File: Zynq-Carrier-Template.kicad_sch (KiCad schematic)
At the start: 5 parts, among them J1 Zynq_SoM

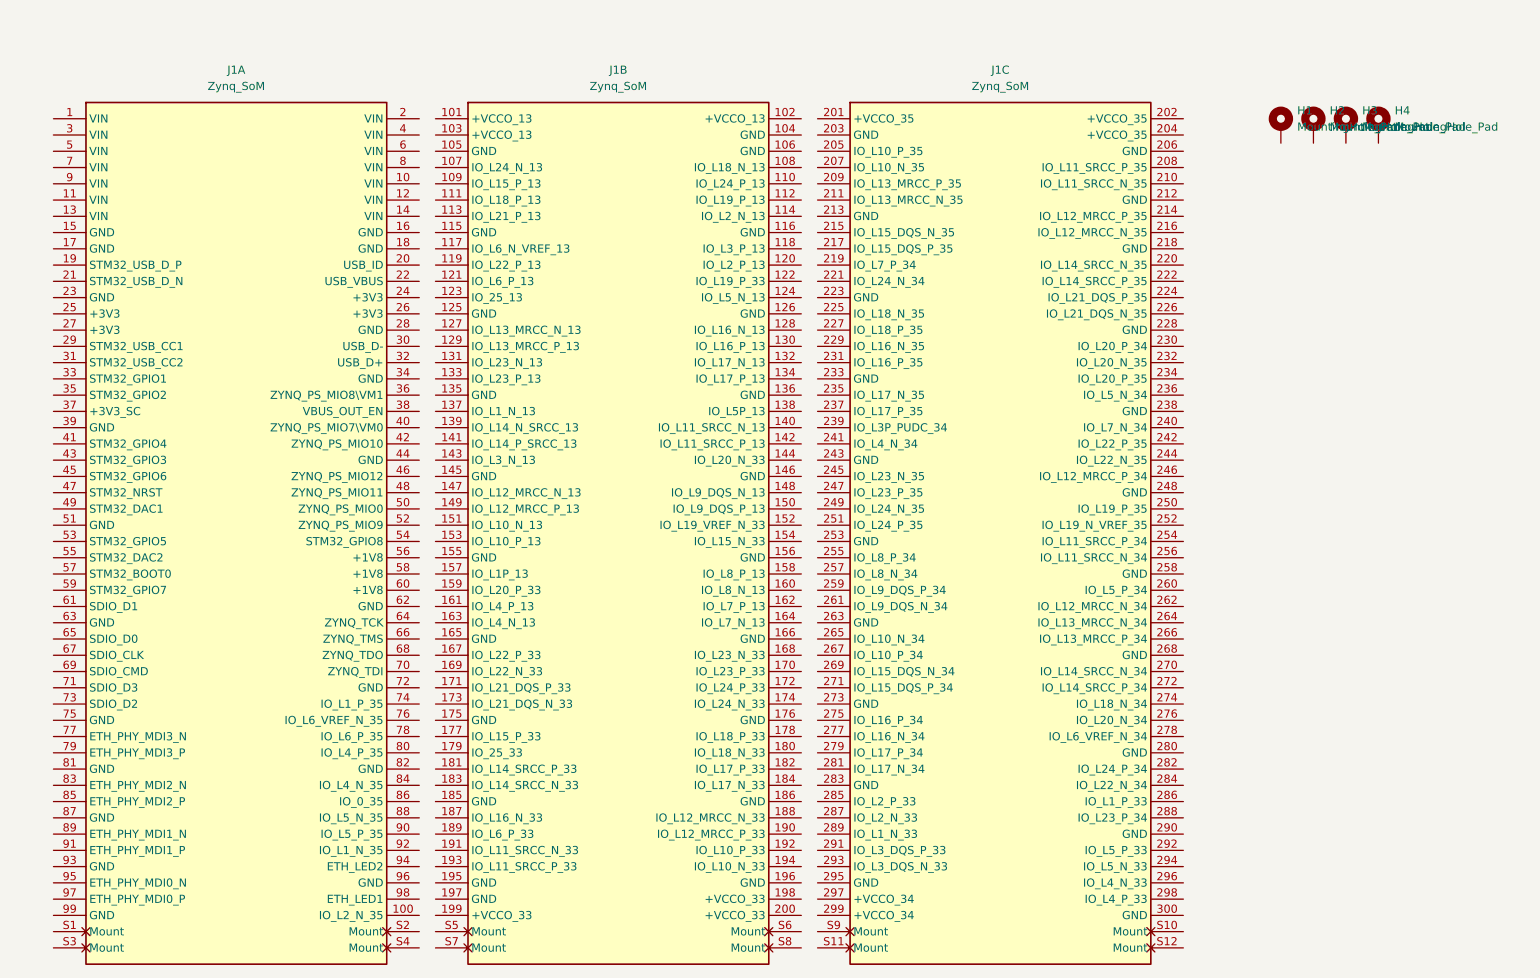
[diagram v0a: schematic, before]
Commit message: Renamed and Updated Silkscreen
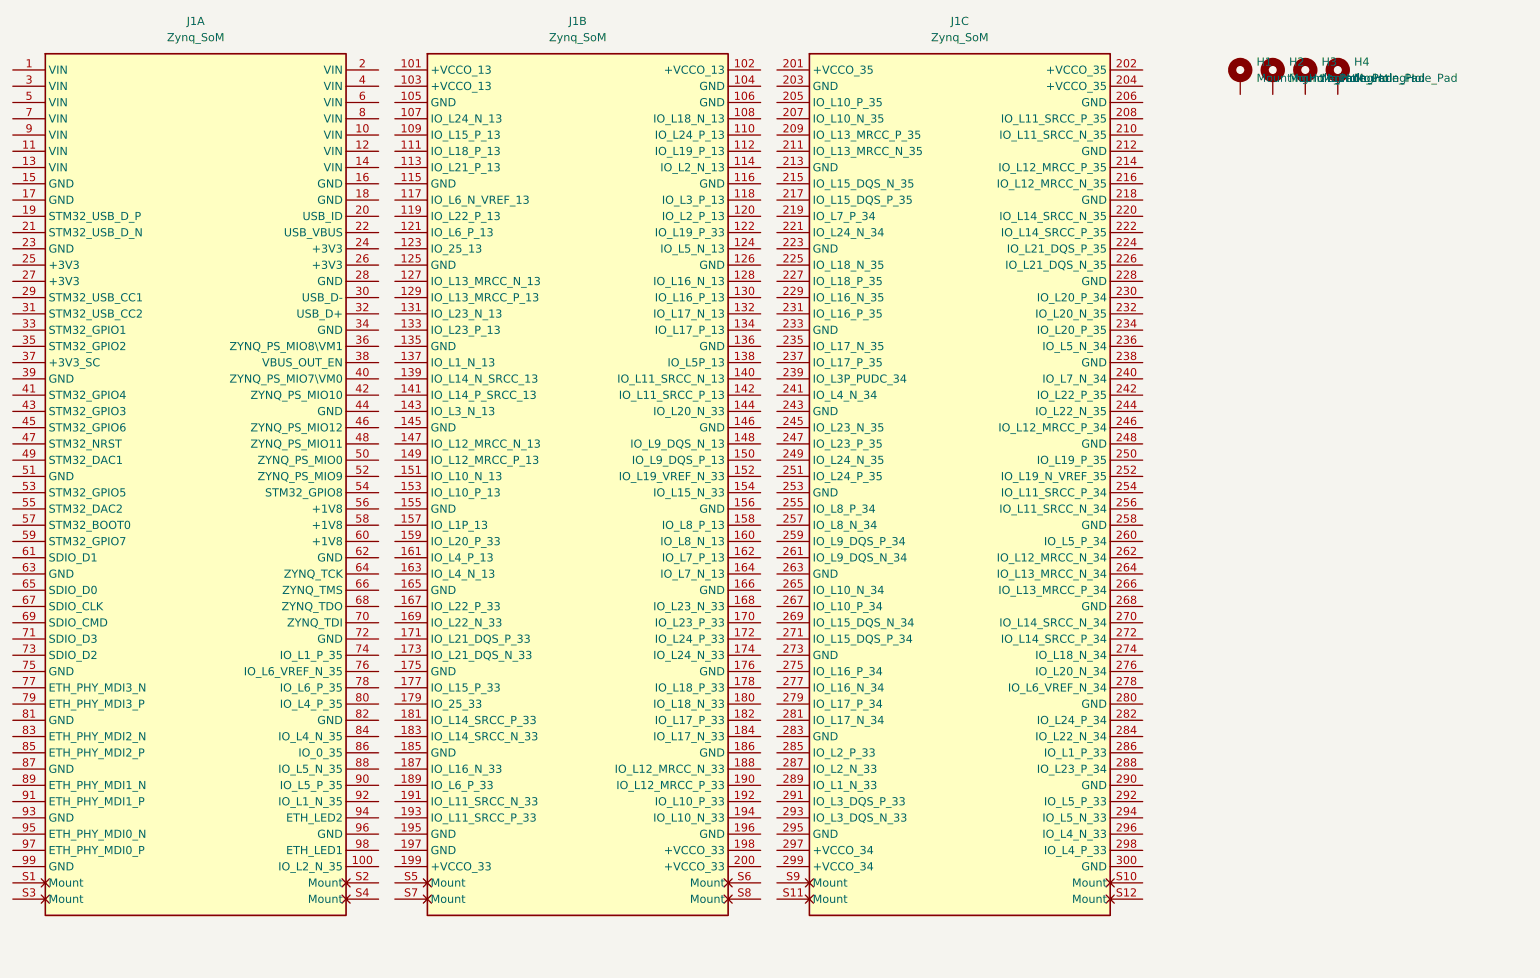
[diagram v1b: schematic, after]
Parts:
- J1: footprint footprint_Zynq_SoM:Zync_SoM -> footprint_Zynq_SoM:Zynq_SoM
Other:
- moved on the sheet: H1, H2, H3, H4, J1A, J1B, J1C
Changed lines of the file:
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@@
 	(symbol
 		(lib_id "Mechanical:MountingHole_Pad")
-		(at 220.98 36.83 0)
+		(at 214.63 29.21 0)
 		(unit 1)
 		(exclude_from_sim yes)
@@
 		(fields_autoplaced yes)
 		(property "Reference" "H1"
-			(at 223.52 34.2899 0)
+			(at 217.17 26.6699 0)
 			(effects
 				(font
@@
 		)
 		(property "Value" "MountingHole_Pad"
-			(at 223.52 36.8299 0)
+			(at 217.17 29.2099 0)
 			(effects
 				(font
@@
 		)
 		(property "Footprint" "MountingHole:MountingHole_2.5mm_Pad_TopBottom"
-			(at 220.98 36.83 0)
+			(at 214.63 29.21 0)
 			(effects
 				(font
@@
 		)
 		(property "Datasheet" "~"
-			(at 220.98 36.83 0)
+			(at 214.63 29.21 0)
 			(effects
 				(font
@@
 		)
 		(property "Description" "Mounting Hole with connection"
-			(at 220.98 36.83 0)
+			(at 214.63 29.21 0)
 			(effects
 				(font
@@
 	(symbol
 		(lib_id "symbol_Zynq_SoM:Zynq_SoM")
-		(at 88.9 35.56 0)
+		(at 82.55 27.94 0)
 		(unit 2)
 		(exclude_from_sim no)
@@
 		(fields_autoplaced yes)
 		(property "Reference" "J1"
-			(at 117.475 27.94 0)
+			(at 111.125 20.32 0)
 			(effects
 				(font
@@
 		)
 		(property "Value" "Zynq_SoM"
-			(at 117.475 30.48 0)
-			(effects
-				(font
-					(size 1.27 1.27)
-				)
-			)
-		)
-		(property "Footprint" "footprint_Zynq_SoM:Zync_SoM"
-			(at 93.98 34.29 0)
+			(at 111.125 22.86 0)
+			(effects
+				(font
+					(size 1.27 1.27)
+				)
+			)
+		)
+		(property "Footprint" "footprint_Zynq_SoM:Zynq_SoM"
+			(at 87.63 26.67 0)
 			(effects
 				(font
@@
 		)
 		(property "Datasheet" ""
-			(at 93.98 39.37 0)
+			(at 87.63 31.75 0)
 			(effects
 				(font
@@
 		)
 		(property "Description" ""
-			(at 88.9 35.56 0)
+			(at 82.55 27.94 0)
 			(effects
 				(font
@@
 	(symbol
 		(lib_id "symbol_Zynq_SoM:Zynq_SoM")
-		(at 29.21 35.56 0)
+		(at 22.86 27.94 0)
 		(unit 1)
 		(exclude_from_sim no)
@@
 		(fields_autoplaced yes)
 		(property "Reference" "J1"
-			(at 57.785 27.94 0)
+			(at 51.435 20.32 0)
 			(effects
 				(font
@@
 		)
 		(property "Value" "Zynq_SoM"
-			(at 57.785 30.48 0)
-			(effects
-				(font
-					(size 1.27 1.27)
-				)
-			)
-		)
-		(property "Footprint" "footprint_Zynq_SoM:Zync_SoM"
-			(at 34.29 34.29 0)
+			(at 51.435 22.86 0)
+			(effects
+				(font
+					(size 1.27 1.27)
+				)
+			)
+		)
+		(property "Footprint" "footprint_Zynq_SoM:Zynq_SoM"
+			(at 27.94 26.67 0)
 			(effects
 				(font
@@
 		)
 		(property "Datasheet" ""
-			(at 34.29 39.37 0)
+			(at 27.94 31.75 0)
 			(effects
 				(font
@@
 		)
 		(property "Description" ""
-			(at 29.21 35.56 0)
+			(at 22.86 27.94 0)
 			(effects
 				(font
@@
 	(symbol
 		(lib_id "Mechanical:MountingHole_Pad")
-		(at 226.06 36.83 0)
+		(at 219.71 29.21 0)
 		(unit 1)
 		(exclude_from_sim yes)
@@
 		(fields_autoplaced yes)
 		(property "Reference" "H2"
-			(at 228.6 34.2899 0)
+			(at 222.25 26.6699 0)
 			(effects
 				(font
@@
 		)
 		(property "Value" "MountingHole_Pad"
-			(at 228.6 36.8299 0)
+			(at 222.25 29.2099 0)
 			(effects
 				(font
@@
 		)
 		(property "Footprint" "MountingHole:MountingHole_2.5mm_Pad_TopBottom"
-			(at 226.06 36.83 0)
+			(at 219.71 29.21 0)
 			(effects
 				(font
@@
 		)
 		(property "Datasheet" "~"
-			(at 226.06 36.83 0)
+			(at 219.71 29.21 0)
 			(effects
 				(font
@@
 		)
 		(property "Description" "Mounting Hole with connection"
-			(at 226.06 36.83 0)
+			(at 219.71 29.21 0)
 			(effects
 				(font
@@
 	(symbol
 		(lib_id "symbol_Zynq_SoM:Zynq_SoM")
-		(at 148.59 35.56 0)
+		(at 142.24 27.94 0)
 		(unit 3)
 		(exclude_from_sim no)
@@
 		(fields_autoplaced yes)
 		(property "Reference" "J1"
-			(at 177.165 27.94 0)
+			(at 170.815 20.32 0)
 			(effects
 				(font
@@
 		)
 		(property "Value" "Zynq_SoM"
-			(at 177.165 30.48 0)
-			(effects
-				(font
-					(size 1.27 1.27)
-				)
-			)
-		)
-		(property "Footprint" "footprint_Zynq_SoM:Zync_SoM"
-			(at 153.67 34.29 0)
+			(at 170.815 22.86 0)
+			(effects
+				(font
+					(size 1.27 1.27)
+				)
+			)
+		)
+		(property "Footprint" "footprint_Zynq_SoM:Zynq_SoM"
+			(at 147.32 26.67 0)
 			(effects
 				(font
@@
 		)
 		(property "Datasheet" ""
-			(at 153.67 39.37 0)
+			(at 147.32 31.75 0)
 			(effects
 				(font
@@
 		)
 		(property "Description" ""
-			(at 148.59 35.56 0)
+			(at 142.24 27.94 0)
 			(effects
 				(font
@@
 	(symbol
 		(lib_id "Mechanical:MountingHole_Pad")
-		(at 236.22 36.83 0)
+		(at 229.87 29.21 0)
 		(unit 1)
 		(exclude_from_sim yes)
@@
 		(fields_autoplaced yes)
 		(property "Reference" "H4"
-			(at 238.76 34.2899 0)
+			(at 232.41 26.6699 0)
 			(effects
 				(font
@@
 		)
 		(property "Value" "MountingHole_Pad"
-			(at 238.76 36.8299 0)
+			(at 232.41 29.2099 0)
 			(effects
 				(font
@@
 		)
 		(property "Footprint" "MountingHole:MountingHole_2.5mm_Pad_TopBottom"
-			(at 236.22 36.83 0)
+			(at 229.87 29.21 0)
 			(effects
 				(font
@@
 		)
 		(property "Datasheet" "~"
-			(at 236.22 36.83 0)
+			(at 229.87 29.21 0)
 			(effects
 				(font
@@
 		)
 		(property "Description" "Mounting Hole with connection"
-			(at 236.22 36.83 0)
+			(at 229.87 29.21 0)
 			(effects
 				(font
@@
 	(symbol
 		(lib_id "Mechanical:MountingHole_Pad")
-		(at 231.14 36.83 0)
+		(at 224.79 29.21 0)
 		(unit 1)
 		(exclude_from_sim yes)
@@
 		(fields_autoplaced yes)
 		(property "Reference" "H3"
-			(at 233.68 34.2899 0)
+			(at 227.33 26.6699 0)
 			(effects
 				(font
@@
 		)
 		(property "Value" "MountingHole_Pad"
-			(at 233.68 36.8299 0)
+			(at 227.33 29.2099 0)
 			(effects
 				(font
@@
 		)
 		(property "Footprint" "MountingHole:MountingHole_2.5mm_Pad_TopBottom"
-			(at 231.14 36.83 0)
+			(at 224.79 29.21 0)
 			(effects
 				(font
@@
 		)
 		(property "Datasheet" "~"
-			(at 231.14 36.83 0)
+			(at 224.79 29.21 0)
 			(effects
 				(font
@@
 		)
 		(property "Description" "Mounting Hole with connection"
-			(at 231.14 36.83 0)
-			(effects
-				(font
+			(at 224.79 29.21 0)
+			(effects
+				(font

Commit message: Squashed commit of the following:
commit 0ad81e69922d32d90721302da68770b5998e2075
Author: pixelatedknight27 <97324570+pixelatedknight27@users.noreply.github.com>
Date:   Wed Aug 6 21:23:02 2025 -0700

    Updated Schematic Switching Regulator Output

commit 8c5282f5a799869a6680777a751af97c305c1966
Author: pixelatedknight27 <maxgross72@gmail.com>
Date:   Wed Jul 30 20:10:45 2025 -0700

    Update Zynq-Carrier-Template.kicad_sch

commit 26cabaedd7311c8d419e12e3f1b26bb927437d1c
Author: pixelatedknight27 <maxgross72@gmail.com>
Date:   Mon Jul 28 15:39:58 2025 -0700

    USB-C Schematic

commit 567233bdd00da02cf27e0d5899afb089722db7fc
Author: eryn-chen <eryncchen@gmail.com>
Date:   Mon Jul 28 14:22:40 2025 -0700

    Import JST_Pins and Inductor

commit 3602218fdc51fd4931fe5a5e7236fe1a478a1e89
Author: pixelatedknight27 <maxgross72@gmail.com>
Date:   Mon Jul 28 13:23:57 2025 -0700

    Added USB-C 3D Model

commit c19733a7ca3310077a98ec0354747d6a3ff68208
Author: eryn-chen <eryncchen@gmail.com>
Date:   Mon Jul 28 12:24:48 2025 -0700

    Import 1uH Inductor

commit dad55b1c15193570489f17efb0b30454465aa197
Author: eryn-chen <eryncchen@gmail.com>
Date:   Sat Jul 26 14:08:40 2025 -0700

    3D Model BQ25629RYKR

commit dfd47739e77adc946db50dcb065d6cd1934a3439
Author: pixelatedknight27 <maxgross72@gmail.com>
Date:   Sat Jul 26 13:56:00 2025 -0700

    Copper Fill demo

commit f9846dcb156c9f426159bf7a8c796c584a4552c7
Author: eryn-chen <eryncchen@gmail.com>
Date:   Sat Jul 26 13:32:59 2025 -0700

    Import BQ25629RYKR

commit 6a2dc9275e746e519794c77d9ef984bae5f9a809
Author: pixelatedknight27 <maxgross72@gmail.com>
Date:   Sat Jul 26 12:43:25 2025 -0700

    Testing collab functionality
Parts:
- added C1, C3, C5: 10uf, Capacitor_SMD:C_0603_1608Metric, symbol Device:C
- added C2, C4, C6: 0.1uf, Capacitor_SMD:C_0603_1608Metric, symbol Device:C
- added C7: 4.7 uF, Capacitor_SMD:C_0603_1608Metric, symbol Device:C_Small
- added C8: 47 nF, Capacitor_SMD:C_0603_1608Metric, symbol Device:C_Small
- added D1: LED, LED_SMD:LED_0805_2012Metric, symbol Device:LED
- added J10: Barrel_Jack_MountingPin, Connector_BarrelJack:BarrelJack_Horizontal, symbol Connector:Barrel_Jack_MountingPin
- added J2: B2B-PH-K-S, JST_Pins:CONN2_B2B-PH-K-S_JST, symbol JST_Pins:B2B-PH-K-S
- added J3: USB_C_Receptacle_USB2.0_16P, Connector_USB:USB_C_Receptacle_G-Switch_GT-USB-7010ASV, symbol Connector:USB_C_Receptacle_USB2.0_16P
- added J4, J5, J6, J9: Conn_01x03, Connector_PinHeader_2.54mm:PinHeader_1x03_P2.54mm_Vertical, symbol Connector_Generic:Conn_01x03
- added J7, J8: Conn_01x02, Connector_PinHeader_2.54mm:PinHeader_1x02_P2.54mm_Vertical, symbol Connector_Generic:Conn_01x02
- added L1: L, Inductor_SMD:L_1008_2520Metric_Pad1.43x2.20mm_HandSolder, symbol Device:L
- added R1, R2, R3: 5.1k, Resistor_SMD:R_0603_1608Metric, symbol Device:R_US
- added R10, R7: 10K, Resistor_SMD:R_0603_1608Metric, symbol Device:R_US
- added R11, R8, R9: 4.7k, Resistor_SMD:R_0603_1608Metric, symbol Device:R_US
- added R4: 1M, Resistor_SMD:R_0603_1608Metric, symbol Device:R_US
- added R5: 100k, Resistor_SMD:R_0603_1608Metric, symbol Device:R_US
- added R6: 330, Resistor_SMD:R_0603_1608Metric, symbol Device:R_US
- added U1: BQ25629RYKR, BQ25629RYKR:RYK0018A-MFG, symbol BQ25629RYKR:BQ25629RYKR
- added U12: SRV05-4, Package_TO_SOT_SMD:SOT-23-6, symbol Power_Protection:SRV05-4
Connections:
- net GND: now reaches H1.1
- net GND: now also H2.1, H3.1, H4.1, J1.104 (GND), J1.105 (GND), J1.106 (GND), J1.115 (GND), J1.116 (GND), J1.125 (GND), J1.126 (GND), J1.135 (GND), J1.136 (GND), J1.145 (GND), J1.146 (GND), J1.15 (GND), J1.155 (GND), J1.16 (GND), J1.165 (GND), J1.166 (GND), J1.17 (GND), J1.175 (GND), J1.176 (GND), J1.18 (GND), J1.185 (GND), J1.186 (GND), J1.195 (GND), J1.196 (GND), J1.197 (GND), J1.203 (GND), J1.206 (GND), J1.213 (GND), J1.218 (GND), J1.223 (GND), J1.228 (GND), J1.23 (GND), J1.233 (GND), J1.238 (GND), J1.243 (GND), J1.248 (GND), J1.253 (GND), J1.258 (GND), J1.263 (GND), J1.268 (GND), J1.273 (GND), J1.28 (GND), J1.280 (GND), J1.283 (GND), J1.290 (GND), J1.295 (GND), J1.300 (GND), J1.39 (GND), J1.44 (GND), J1.51 (GND), J1.62 (GND), J1.63 (GND), J1.72 (GND), J1.75 (GND), J1.81 (GND), J1.82 (GND), J1.87 (GND), J1.96 (GND), J1.99 (GND), C1.2, C2.2, C3.2, C4.2, C5.2, C6.2, C7.2, D1.1 (K), J10.2, J10.MP (MountPin), J2.1, J3.A1 (GND), J3.A12 (GND), J3.B1 (GND), J3.B12 (GND), J6.3 (Pin_3), R1.1, R2.1, R4.2, R5.2, U1.15 (GND), U1.6 (TS), U12.2 (VN)
- net +5V: now reaches J1.1 (VIN)
- net +5V: now also J1.10 (VIN), J1.11 (VIN), J1.12 (VIN), J1.13 (VIN), J1.14 (VIN), J1.2 (VIN), J1.3 (VIN), J1.4 (VIN), J1.5 (VIN), J1.6 (VIN), J1.7 (VIN), J1.8 (VIN), J1.9 (VIN), J9.2 (Pin_2), R11.2, R8.1, R9.1
- net USB_SOM_D-: now reaches J1.30 (USB_D-)
- net USB_SOM_D-: now also J4.3 (Pin_3)
- net USB_SOM_D+: now reaches J1.32 (USB_D+)
- net USB_SOM_D+: now also J5.3 (Pin_3)
- new net: J3.A5 (CC1), R1.2
- new net: J3.B5 (CC2), R2.2
- new net: J3.S1 (SHIELD), R4.1
- new net: J7.1 (Pin_1), R8.2
- new net: C8.2, U1.1 (BTST)
- new net: R6.1, U1.10 (STAT)
- new net: C8.1, L1.1, U1.16 (SW)
- new net: C1.1, C2.1, U1.17 (PMID)
- new net: C7.1, U1.2 (REGN)
- new net: J8.1 (Pin_1), R9.2
- new net: R3.2, U12.5 (VP)
- new net: D1.2 (A), R6.2
- new net: J6.1 (Pin_1), R7.2
- new net: J6.2 (Pin_2), R10.2
- new net SCL: J7.2 (Pin_2), R7.1, U1.13 (SCL)
- new net SDA: J8.2 (Pin_2), R10.1, U1.12 (SDA)
- new net USB_D+: J3.A6 (D+), J3.B6 (D+), J5.2 (Pin_2), U12.3 (IO2)
- new net USB_D-: J3.A7 (D-), J3.B7 (D-), J4.2 (Pin_2), U12.1 (IO1)
- new net USB_POW_D+: J5.1 (Pin_1), U1.5 (D+)
- new net USB_POW_D-: J4.1 (Pin_1), U1.4 (D-)
- new net VBAT: J2.2, U1.8 (BAT)
- new net VREG_OUT: J9.1 (Pin_1), L1.2, U1.9 (SYS)
- new net V_USB: C3.1, C4.1, C5.1, C6.1, J3.A4 (VBUS), J3.A9 (VBUS), J3.B4 (VBUS), J3.B9 (VBUS), R3.1, R5.1, U1.18 (VBUS)
- new net Vps: J10.1, J9.3 (Pin_3)
- new net ~{CSn}: R11.1, U1.14 (CE_N)
- no-connect marks 0 -> 7
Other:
- note added: "Place close to VBUS pin"
- moved on the sheet: H1, H2, H3, H4, J1A, J1B, J1C
